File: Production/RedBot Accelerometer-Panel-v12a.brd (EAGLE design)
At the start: 129 x 137.2 mm, 915 parts, among them U1 MMA8452QMMA8452Q-1:1, U10 PCA9306, U100 PCA9306, U101 MMA8452QMMA8452Q-1:1, U102 MIC5205-3.3V, U103 PCA9306, U104 MMA8452QMMA8452Q-1:1, U105 MIC5205-3.3V, U106 PCA9306, U107 MMA8452QMMA8452Q-1:1, U108 MIC5205-3.3V, U109 PCA9306, U11 MMA8452QMMA8452Q-1:1, U110 MMA8452QMMA8452Q-1:1, U111 MIC5205-3.3V, U112 PCA9306, U113 MMA8452QMMA8452Q-1:1, U114 MIC5205-3.3V, U115 PCA9306, U116 MMA8452QMMA8452Q-1:1, U117 MIC5205-3.3V, U118 PCA9306, U119 MMA8452QMMA8452Q-1:1, U12 MIC5205-3.3V, U120 MIC5205-3.3V, U121 PCA9306, U122 MMA8452QMMA8452Q-1:1, U123 MIC5205-3.3V, U124 PCA9306, U125 MMA8452QMMA8452Q-1:1, U126 MIC5205-3.3V, U127 PCA9306, U128 MMA8452QMMA8452Q-1:1, U129 MIC5205-3.3V, U13 PCA9306, U130 PCA9306, U131 MMA8452QMMA8452Q-1:1, U132 MIC5205-3.3V, U133 PCA9306, U134 MMA8452QMMA8452Q-1:1, U135 MIC5205-3.3V, U136 PCA9306, U137 MMA8452QMMA8452Q-1:1, U138 MIC5205-3.3V, U139 PCA9306, U14 MMA8452QMMA8452Q-1:1, U140 MMA8452QMMA8452Q-1:1, U141 MIC5205-3.3V, U142 PCA9306, U143 MMA8452QMMA8452Q-1:1, U144 MIC5205-3.3V, U15 MIC5205-3.3V, U16 PCA9306, U17 MMA8452QMMA8452Q-1:1, U18 MIC5205-3.3V, U19 PCA9306, U2 MIC5205-3.3V, U20 MMA8452QMMA8452Q-1:1, U21 MIC5205-3.3V, U22 PCA9306, U23 MMA8452QMMA8452Q-1:1, U24 MIC5205-3.3V, U25 PCA9306, U26 MMA8452QMMA8452Q-1:1, U27 MIC5205-3.3V, U28 PCA9306, U29 MMA8452QMMA8452Q-1:1, U3 PCA9306, U30 MIC5205-3.3V, U31 PCA9306, U32 MMA8452QMMA8452Q-1:1, U33 MIC5205-3.3V, U34 PCA9306, U35 MMA8452QMMA8452Q-1:1, U36 MIC5205-3.3V, U37 PCA9306, U38 MMA8452QMMA8452Q-1:1, U39 MIC5205-3.3V, U4 PCA9306, U40 PCA9306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

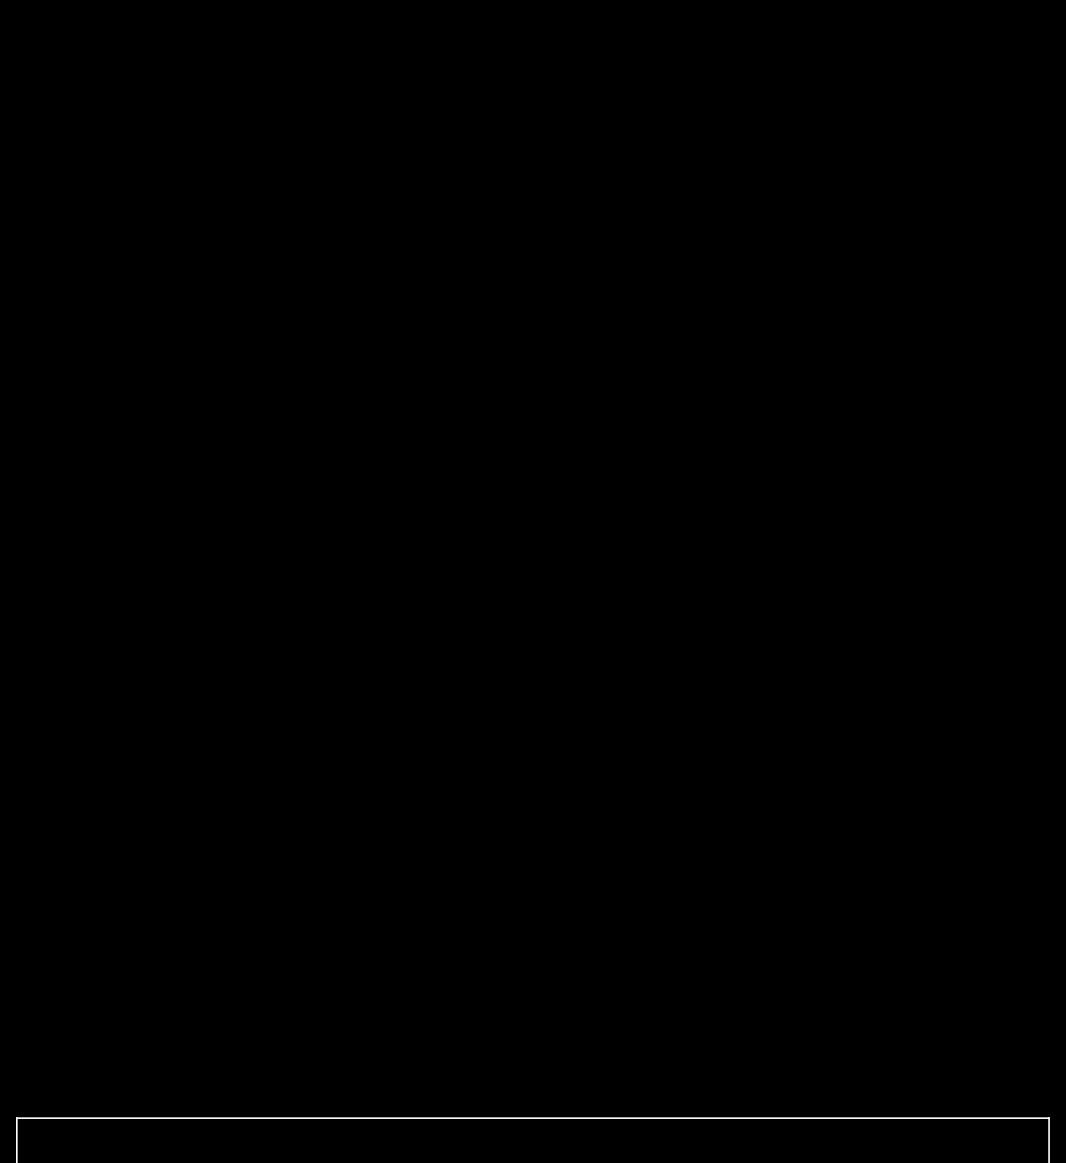
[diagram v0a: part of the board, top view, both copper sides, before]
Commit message: created large v12a panel
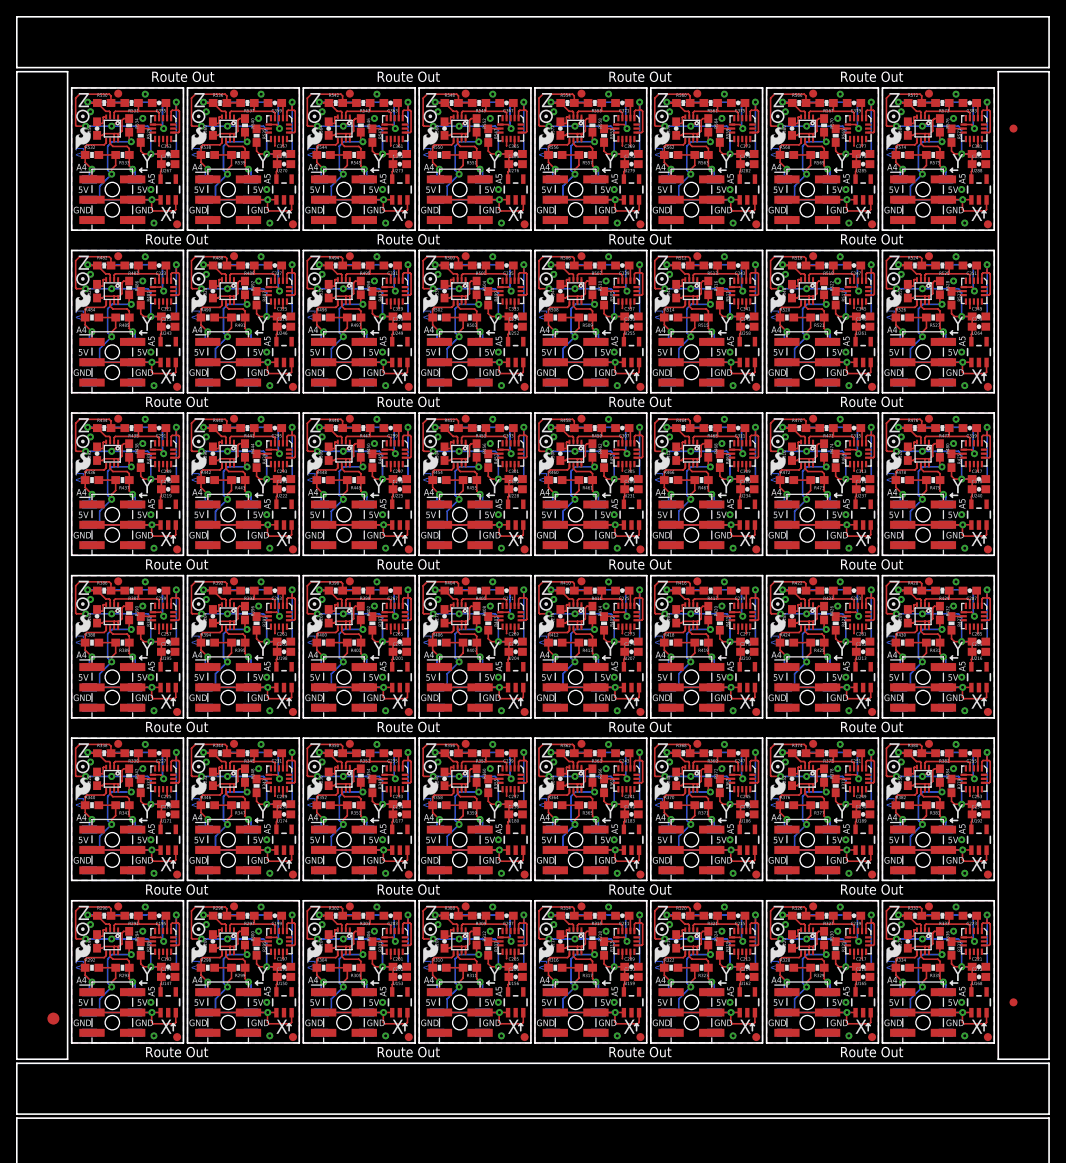
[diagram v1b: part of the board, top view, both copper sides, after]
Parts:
- added C193, C195, C196, C197, C199, C200, C201, C203, C204, C205, C207, C208, C209, C211, C212, C213, C215, C216, C217, C219, C220, C221, C223, C224, C225, C227, C228, C229, C231, C232, C233, C235, C236, C237, C239, C240, C241, C243, C244, C245, C247, C248, C249, C251, C252, C253, C255, C256, C257, C259, C260, C261, C263, C264, C265, C267, C268, C269, C271, C272, C273, C275, C276, C277, C279, C280, C281, C283, C284, C285, C287, C288, C289, C291, C292, C293, C295, C296, C297, C299, C300, C301, C303, C304, C305, C307, C308, C309, C311, C312, C313, C315, C316, C317, C319, C320, C321, C323, C324, C325, C327, C328, C329, C331, C332, C333, C335, C336, C337, C339, C340, C341, C343, C344, C345, C347, C348, C349, C351, C352, C353, C355, C356, C357, C359, C360, C361, C363, C364, C365, C367, C368, C369, C371, C372, C373, C375, C376, C377, C379, C380, C381, C383, C384: 0.1uF, SparkFun-Capacitors:0603-CAP
- added C194, C198, C202, C206, C210, C214, C218, C222, C226, C230, C234, C238, C242, C246, C250, C254, C258, C262, C266, C270, C274, C278, C282, C286, C290, C294, C298, C302, C306, C310, C314, C318, C322, C326, C330, C334, C338, C342, C346, C350, C354, C358, C362, C366, C370, C374, C378, C382: 4.7uF, SparkFun-Capacitors:0603-CAP
- added E$4, E$5: (no value), SparkFun-Aesthetics:FIDUCIAL-1X2
- added E$6: (no value), SparkFun-Retired:FIDUCIAL-1.5X3
- added FID100, FID101, FID102, FID103, FID104, FID105, FID106, FID107, FID108, FID109, FID110, FID111, FID112, FID113, FID114, FID115, FID116, FID117, FID118, FID119, FID120, FID121, FID122, FID123, FID124, FID125, FID126, FID127, FID128, FID129, FID130, FID131, FID132, FID133, FID134, FID135, FID136, FID137, FID138, FID139, FID140, FID141, FID142, FID143, FID144, FID145, FID146, FID147, FID148, FID149, FID150, FID151, FID152, FID153, FID154, FID155, FID156, FID157, FID158, FID159, FID160, FID161, FID162, FID163, FID164, FID165, FID166, FID167, FID168, FID169, FID170, FID171, FID172, FID173, FID174, FID175, FID176, FID177, FID178, FID179, FID180, FID181, FID182, FID183, FID184, FID185, FID186, FID187, FID188, FID189, FID190, FID191, FID192, FID97, FID98, FID99: FIDUCIAL1X2, SparkFun-Aesthetics:FIDUCIAL-1X2
- added JP100, JP102, JP104, JP106, JP108, JP110, JP112, JP114, JP116, JP118, JP120, JP122, JP124, JP126, JP128, JP130, JP132, JP134, JP136, JP138, JP140, JP142, JP144, JP146, JP148, JP150, JP152, JP154, JP156, JP158, JP160, JP162, JP164, JP166, JP168, JP170, JP172, JP174, JP176, JP178, JP180, JP182, JP184, JP186, JP188, JP190, JP192, JP98: (no value), SparkFun-Connectors:2X3_SMD
- added JP101, JP103, JP105, JP107, JP109, JP111, JP113, JP115, JP117, JP119, JP121, JP123, JP125, JP127, JP129, JP131, JP133, JP135, JP137, JP139, JP141, JP143, JP145, JP147, JP149, JP151, JP153, JP155, JP157, JP159, JP161, JP163, JP165, JP167, JP169, JP171, JP173, JP175, JP177, JP179, JP181, JP183, JP185, JP187, JP189, JP191, JP97, JP99: (no value), SparkFun-Connectors:2X3_SMT_POSTS
- added LOGO100, LOGO102, LOGO104, LOGO106, LOGO108, LOGO110, LOGO112, LOGO114, LOGO116, LOGO118, LOGO120, LOGO122, LOGO124, LOGO126, LOGO128, LOGO130, LOGO132, LOGO134, LOGO136, LOGO138, LOGO140, LOGO142, LOGO144, LOGO146, LOGO148, LOGO150, LOGO152, LOGO154, LOGO156, LOGO158, LOGO160, LOGO162, LOGO164, LOGO166, LOGO168, LOGO170, LOGO172, LOGO174, LOGO176, LOGO178, LOGO180, LOGO182, LOGO184, LOGO186, LOGO188, LOGO190, LOGO192, LOGO98: OSHW-LOGOS, SparkFun-Aesthetics:OSHW-LOGO-S
- added LOGO101, LOGO103, LOGO105, LOGO107, LOGO109, LOGO111, LOGO113, LOGO115, LOGO117, LOGO119, LOGO121, LOGO123, LOGO125, LOGO127, LOGO129, LOGO131, LOGO133, LOGO135, LOGO137, LOGO139, LOGO141, LOGO143, LOGO145, LOGO147, LOGO149, LOGO151, LOGO153, LOGO155, LOGO157, LOGO159, LOGO161, LOGO163, LOGO165, LOGO167, LOGO169, LOGO171, LOGO173, LOGO175, LOGO177, LOGO179, LOGO181, LOGO183, LOGO185, LOGO187, LOGO189, LOGO191, LOGO97, LOGO99: LOGO-SFESK, SparkFun-Aesthetics:SFE-LOGO-FLAME
- added R289, R295, R301, R307, R313, R319, R325, R331, R337, R343, R349, R355, R361, R367, R373, R379, R385, R391, R397, R403, R409, R415, R421, R427, R433, R439, R445, R451, R457, R463, R469, R475, R481, R487, R493, R499, R505, R511, R517, R523, R529, R535, R541, R547, R553, R559, R565, R571: 10k, SparkFun-Resistors:0603-RES
- added R290, R291, R292, R293, R296, R297, R298, R299, R302, R303, R304, R305, R308, R309, R310, R311, R314, R315, R316, R317, R320, R321, R322, R323, R326, R327, R328, R329, R332, R333, R334, R335, R338, R339, R340, R341, R344, R345, R346, R347, R350, R351, R352, R353, R356, R357, R358, R359, R362, R363, R364, R365, R368, R369, R370, R371, R374, R375, R376, R377, R380, R381, R382, R383, R386, R387, R388, R389, R392, R393, R394, R395, R398, R399, R400, R401, R404, R405, R406, R407, R410, R411, R412, R413, R416, R417, R418, R419, R422, R423, R424, R425, R428, R429, R430, R431, R434, R435, R436, R437, R440, R441, R442, R443, R446, R447, R448, R449, R452, R453, R454, R455, R458, R459, R460, R461, R464, R465, R466, R467, R470, R471, R472, R473, R476, R477, R478, R479, R482, R483, R484, R485, R488, R489, R490, R491, R494, R495, R496, R497, R500, R501, R502, R503, R506, R507, R508, R509, R512, R513, R514, R515, R518, R519, R520, R521, R524, R525, R526, R527, R530, R531, R532, R533, R536, R537, R538, R539, R542, R543, R544, R545, R548, R549, R550, R551, R554, R555, R556, R557, R560, R561, R562, R563, R566, R567, R568, R569, R572, R573, R574, R575: 1k, SparkFun-Resistors:0603-RES
- added R294, R300, R306, R312, R318, R324, R330, R336, R342, R348, R354, R360, R366, R372, R378, R384, R390, R396, R402, R408, R414, R420, R426, R432, R438, R444, R450, R456, R462, R468, R474, R480, R486, R492, R498, R504, R510, R516, R522, R528, R534, R540, R546, R552, R558, R564, R570, R576: 200k, SparkFun-Resistors:0603-RES
- added U145, U148, U151, U154, U157, U160, U163, U166, U169, U172, U175, U178, U181, U184, U187, U190, U193, U196, U199, U202, U205, U208, U211, U214, U217, U220, U223, U226, U229, U232, U235, U238, U241, U244, U247, U250, U253, U256, U259, U262, U265, U268, U271, U274, U277, U280, U283, U286: PCA9306, SparkFun-DigitalIC:PCA9306DC-1:1
- added U146, U149, U152, U155, U158, U161, U164, U167, U170, U173, U176, U179, U182, U185, U188, U191, U194, U197, U200, U203, U206, U209, U212, U215, U218, U221, U224, U227, U230, U233, U236, U239, U242, U245, U248, U251, U254, U257, U260, U263, U266, U269, U272, U275, U278, U281, U284, U287: MMA8452QMMA8452Q-1:1, SparkFun-Sensors:MMA8452Q-1:1
- added U147, U150, U153, U156, U159, U162, U165, U168, U171, U174, U177, U180, U183, U186, U189, U192, U195, U198, U201, U204, U207, U210, U213, U216, U219, U222, U225, U228, U231, U234, U237, U240, U243, U246, U249, U252, U255, U258, U261, U264, U267, U270, U273, U276, U279, U282, U285, U288: MIC5205-3.3V, SparkFun-PowerIC:SOT23-5
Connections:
- new net 3.3V48: C193.1, C194.1, R289.2, R290.2, R291.2, U145.1, U146.1, U146.14, U147.5
- new net 3.3V49: C197.1, C198.1, R295.2, R296.2, R297.2, U148.1, U149.1, U149.14, U150.5
- new net 3.3V50: C201.1, C202.1, R301.2, R302.2, R303.2, U151.1, U152.1, U152.14, U153.5
- new net 3.3V51: C205.1, C206.1, R307.2, R308.2, R309.2, U154.1, U155.1, U155.14, U156.5
- new net 3.3V52: C209.1, C210.1, R313.2, R314.2, R315.2, U157.1, U158.1, U158.14, U159.5
- new net 3.3V53: C213.1, C214.1, R319.2, R320.2, R321.2, U160.1, U161.1, U161.14, U162.5
- new net 3.3V54: C217.1, C218.1, R325.2, R326.2, R327.2, U163.1, U164.1, U164.14, U165.5
- new net 3.3V55: C221.1, C222.1, R331.2, R332.2, R333.2, U166.1, U167.1, U167.14, U168.5
- new net 3.3V56: C225.1, C226.1, R337.2, R338.2, R339.2, U169.1, U170.1, U170.14, U171.5
- new net 3.3V57: C229.1, C230.1, R343.2, R344.2, R345.2, U172.1, U173.1, U173.14, U174.5
- new net 3.3V58: C233.1, C234.1, R349.2, R350.2, R351.2, U175.1, U176.1, U176.14, U177.5
- new net 3.3V59: C237.1, C238.1, R355.2, R356.2, R357.2, U178.1, U179.1, U179.14, U180.5
- new net 3.3V60: C241.1, C242.1, R361.2, R362.2, R363.2, U181.1, U182.1, U182.14, U183.5
- new net 3.3V61: C245.1, C246.1, R367.2, R368.2, R369.2, U184.1, U185.1, U185.14, U186.5
- new net 3.3V62: C249.1, C250.1, R373.2, R374.2, R375.2, U187.1, U188.1, U188.14, U189.5
- new net 3.3V63: C253.1, C254.1, R379.2, R380.2, R381.2, U190.1, U191.1, U191.14, U192.5
- new net 3.3V64: C257.1, C258.1, R385.2, R386.2, R387.2, U193.1, U194.1, U194.14, U195.5
- new net 3.3V65: C261.1, C262.1, R391.2, R392.2, R393.2, U196.1, U197.1, U197.14, U198.5
- new net 3.3V66: C265.1, C266.1, R397.2, R398.2, R399.2, U199.1, U200.1, U200.14, U201.5
- new net 3.3V67: C269.1, C270.1, R403.2, R404.2, R405.2, U202.1, U203.1, U203.14, U204.5
- new net 3.3V68: C273.1, C274.1, R409.2, R410.2, R411.2, U205.1, U206.1, U206.14, U207.5
- new net 3.3V69: C277.1, C278.1, R415.2, R416.2, R417.2, U208.1, U209.1, U209.14, U210.5
- new net 3.3V70: C281.1, C282.1, R421.2, R422.2, R423.2, U211.1, U212.1, U212.14, U213.5
- new net 3.3V71: C285.1, C286.1, R427.2, R428.2, R429.2, U214.1, U215.1, U215.14, U216.5
- new net 3.3V72: C289.1, C290.1, R433.2, R434.2, R435.2, U217.1, U218.1, U218.14, U219.5
- new net 3.3V73: C293.1, C294.1, R439.2, R440.2, R441.2, U220.1, U221.1, U221.14, U222.5
- new net 3.3V74: C297.1, C298.1, R445.2, R446.2, R447.2, U223.1, U224.1, U224.14, U225.5
- new net 3.3V75: C301.1, C302.1, R451.2, R452.2, R453.2, U226.1, U227.1, U227.14, U228.5
- new net 3.3V76: C305.1, C306.1, R457.2, R458.2, R459.2, U229.1, U230.1, U230.14, U231.5
- new net 3.3V77: C309.1, C310.1, R463.2, R464.2, R465.2, U232.1, U233.1, U233.14, U234.5
- new net 3.3V78: C313.1, C314.1, R469.2, R470.2, R471.2, U235.1, U236.1, U236.14, U237.5
- new net 3.3V79: C317.1, C318.1, R475.2, R476.2, R477.2, U238.1, U239.1, U239.14, U240.5
- new net 3.3V80: C321.1, C322.1, R481.2, R482.2, R483.2, U241.1, U242.1, U242.14, U243.5
- new net 3.3V81: C325.1, C326.1, R487.2, R488.2, R489.2, U244.1, U245.1, U245.14, U246.5
- new net 3.3V82: C329.1, C330.1, R493.2, R494.2, R495.2, U247.1, U248.1, U248.14, U249.5
- new net 3.3V83: C333.1, C334.1, R499.2, R500.2, R501.2, U250.1, U251.1, U251.14, U252.5
- new net 3.3V84: C337.1, C338.1, R505.2, R506.2, R507.2, U253.1, U254.1, U254.14, U255.5
- new net 3.3V85: C341.1, C342.1, R511.2, R512.2, R513.2, U256.1, U257.1, U257.14, U258.5
- new net 3.3V86: C345.1, C346.1, R517.2, R518.2, R519.2, U259.1, U260.1, U260.14, U261.5
- new net 3.3V87: C349.1, C350.1, R523.2, R524.2, R525.2, U262.1, U263.1, U263.14, U264.5
- new net 3.3V88: C353.1, C354.1, R529.2, R530.2, R531.2, U265.1, U266.1, U266.14, U267.5
- new net 3.3V89: C357.1, C358.1, R535.2, R536.2, R537.2, U268.1, U269.1, U269.14, U270.5
- new net 3.3V90: C361.1, C362.1, R541.2, R542.2, R543.2, U271.1, U272.1, U272.14, U273.5
- new net 3.3V91: C365.1, C366.1, R547.2, R548.2, R549.2, U274.1, U275.1, U275.14, U276.5
- new net 3.3V92: C369.1, C370.1, R553.2, R554.2, R555.2, U277.1, U278.1, U278.14, U279.5
- new net 3.3V93: C373.1, C374.1, R559.2, R560.2, R561.2, U280.1, U281.1, U281.14, U282.5
- new net 3.3V94: C377.1, C378.1, R565.2, R566.2, R567.2, U283.1, U284.1, U284.14, U285.5
- new net 3.3V95: C381.1, C382.1, R571.2, R572.2, R573.2, U286.1, U287.1, U287.14, U288.5
- new net 5V48: JP97.3, JP97.4, JP98.3, JP98.4, R292.2, R293.2, R294.2, U147.1, U147.3
- new net 5V49: JP100.3, JP100.4, JP99.3, JP99.4, R298.2, R299.2, R300.2, U150.1, U150.3
- new net 5V50: JP101.3, JP101.4, JP102.3, JP102.4, R304.2, R305.2, R306.2, U153.1, U153.3
- new net 5V51: JP103.3, JP103.4, JP104.3, JP104.4, R310.2, R311.2, R312.2, U156.1, U156.3
- new net 5V52: JP105.3, JP105.4, JP106.3, JP106.4, R316.2, R317.2, R318.2, U159.1, U159.3
- new net 5V53: JP107.3, JP107.4, JP108.3, JP108.4, R322.2, R323.2, R324.2, U162.1, U162.3
- new net 5V54: JP109.3, JP109.4, JP110.3, JP110.4, R328.2, R329.2, R330.2, U165.1, U165.3
- new net 5V55: JP111.3, JP111.4, JP112.3, JP112.4, R334.2, R335.2, R336.2, U168.1, U168.3
- new net 5V56: JP113.3, JP113.4, JP114.3, JP114.4, R340.2, R341.2, R342.2, U171.1, U171.3
- new net 5V57: JP115.3, JP115.4, JP116.3, JP116.4, R346.2, R347.2, R348.2, U174.1, U174.3
- new net 5V58: JP117.3, JP117.4, JP118.3, JP118.4, R352.2, R353.2, R354.2, U177.1, U177.3
- new net 5V59: JP119.3, JP119.4, JP120.3, JP120.4, R358.2, R359.2, R360.2, U180.1, U180.3
- new net 5V60: JP121.3, JP121.4, JP122.3, JP122.4, R364.2, R365.2, R366.2, U183.1, U183.3
- new net 5V61: JP123.3, JP123.4, JP124.3, JP124.4, R370.2, R371.2, R372.2, U186.1, U186.3
- new net 5V62: JP125.3, JP125.4, JP126.3, JP126.4, R376.2, R377.2, R378.2, U189.1, U189.3
- new net 5V63: JP127.3, JP127.4, JP128.3, JP128.4, R382.2, R383.2, R384.2, U192.1, U192.3
- new net 5V64: JP129.3, JP129.4, JP130.3, JP130.4, R388.2, R389.2, R390.2, U195.1, U195.3
- new net 5V65: JP131.3, JP131.4, JP132.3, JP132.4, R394.2, R395.2, R396.2, U198.1, U198.3
- new net 5V66: JP133.3, JP133.4, JP134.3, JP134.4, R400.2, R401.2, R402.2, U201.1, U201.3
- new net 5V67: JP135.3, JP135.4, JP136.3, JP136.4, R406.2, R407.2, R408.2, U204.1, U204.3
- new net 5V68: JP137.3, JP137.4, JP138.3, JP138.4, R412.2, R413.2, R414.2, U207.1, U207.3
- new net 5V69: JP139.3, JP139.4, JP140.3, JP140.4, R418.2, R419.2, R420.2, U210.1, U210.3
- new net 5V70: JP141.3, JP141.4, JP142.3, JP142.4, R424.2, R425.2, R426.2, U213.1, U213.3
- new net 5V71: JP143.3, JP143.4, JP144.3, JP144.4, R430.2, R431.2, R432.2, U216.1, U216.3
- new net 5V72: JP145.3, JP145.4, JP146.3, JP146.4, R436.2, R437.2, R438.2, U219.1, U219.3
- new net 5V73: JP147.3, JP147.4, JP148.3, JP148.4, R442.2, R443.2, R444.2, U222.1, U222.3
- new net 5V74: JP149.3, JP149.4, JP150.3, JP150.4, R448.2, R449.2, R450.2, U225.1, U225.3
- new net 5V75: JP151.3, JP151.4, JP152.3, JP152.4, R454.2, R455.2, R456.2, U228.1, U228.3
- new net 5V76: JP153.3, JP153.4, JP154.3, JP154.4, R460.2, R461.2, R462.2, U231.1, U231.3
- new net 5V77: JP155.3, JP155.4, JP156.3, JP156.4, R466.2, R467.2, R468.2, U234.1, U234.3
- new net 5V78: JP157.3, JP157.4, JP158.3, JP158.4, R472.2, R473.2, R474.2, U237.1, U237.3
- new net 5V79: JP159.3, JP159.4, JP160.3, JP160.4, R478.2, R479.2, R480.2, U240.1, U240.3
- new net 5V80: JP161.3, JP161.4, JP162.3, JP162.4, R484.2, R485.2, R486.2, U243.1, U243.3
- new net 5V81: JP163.3, JP163.4, JP164.3, JP164.4, R490.2, R491.2, R492.2, U246.1, U246.3
- new net 5V82: JP165.3, JP165.4, JP166.3, JP166.4, R496.2, R497.2, R498.2, U249.1, U249.3
- new net 5V83: JP167.3, JP167.4, JP168.3, JP168.4, R502.2, R503.2, R504.2, U252.1, U252.3
- new net 5V84: JP169.3, JP169.4, JP170.3, JP170.4, R508.2, R509.2, R510.2, U255.1, U255.3
- new net 5V85: JP171.3, JP171.4, JP172.3, JP172.4, R514.2, R515.2, R516.2, U258.1, U258.3
- new net 5V86: JP173.3, JP173.4, JP174.3, JP174.4, R520.2, R521.2, R522.2, U261.1, U261.3
- new net 5V87: JP175.3, JP175.4, JP176.3, JP176.4, R526.2, R527.2, R528.2, U264.1, U264.3
- new net 5V88: JP177.3, JP177.4, JP178.3, JP178.4, R532.2, R533.2, R534.2, U267.1, U267.3
- new net 5V89: JP179.3, JP179.4, JP180.3, JP180.4, R538.2, R539.2, R540.2, U270.1, U270.3
- new net 5V90: JP181.3, JP181.4, JP182.3, JP182.4, R544.2, R545.2, R546.2, U273.1, U273.3
- new net 5V91: JP183.3, JP183.4, JP184.3, JP184.4, R550.2, R551.2, R552.2, U276.1, U276.3
- new net 5V92: JP185.3, JP185.4, JP186.3, JP186.4, R556.2, R557.2, R558.2, U279.1, U279.3
- new net 5V93: JP187.3, JP187.4, JP188.3, JP188.4, R562.2, R563.2, R564.2, U282.1, U282.3
- new net 5V94: JP189.3, JP189.4, JP190.3, JP190.4, R568.2, R569.2, R570.2, U285.1, U285.3
- new net 5V95: JP191.3, JP191.4, JP192.3, JP192.4, R574.2, R575.2, R576.2, U288.1, U288.3
- new net ADDR48: R289.1, U146.7
- new net ADDR49: R295.1, U149.7
- new net ADDR50: R301.1, U152.7
- new net ADDR51: R307.1, U155.7
- new net ADDR52: R313.1, U158.7
- new net ADDR53: R319.1, U161.7
- new net ADDR54: R325.1, U164.7
- new net ADDR55: R331.1, U167.7
- new net ADDR56: R337.1, U170.7
- new net ADDR57: R343.1, U173.7
- new net ADDR58: R349.1, U176.7
- new net ADDR59: R355.1, U179.7
- new net ADDR60: R361.1, U182.7
- new net ADDR61: R367.1, U185.7
- new net ADDR62: R373.1, U188.7
- new net ADDR63: R379.1, U191.7
- new net ADDR64: R385.1, U194.7
- new net ADDR65: R391.1, U197.7
- new net ADDR66: R397.1, U200.7
- new net ADDR67: R403.1, U203.7
- new net ADDR68: R409.1, U206.7
- new net ADDR69: R415.1, U209.7
- new net ADDR70: R421.1, U212.7
- new net ADDR71: R427.1, U215.7
- new net ADDR72: R433.1, U218.7
- new net ADDR73: R439.1, U221.7
- new net ADDR74: R445.1, U224.7
- new net ADDR75: R451.1, U227.7
- new net ADDR76: R457.1, U230.7
- new net ADDR77: R463.1, U233.7
- new net ADDR78: R469.1, U236.7
- new net ADDR79: R475.1, U239.7
- new net ADDR80: R481.1, U242.7
- new net ADDR81: R487.1, U245.7
- new net ADDR82: R493.1, U248.7
- new net ADDR83: R499.1, U251.7
- new net ADDR84: R505.1, U254.7
- new net ADDR85: R511.1, U257.7
- new net ADDR86: R517.1, U260.7
- new net ADDR87: R523.1, U263.7
- new net ADDR88: R529.1, U266.7
- new net ADDR89: R535.1, U269.7
- new net ADDR90: R541.1, U272.7
- new net ADDR91: R547.1, U275.7
- new net ADDR92: R553.1, U278.7
- new net ADDR93: R559.1, U281.7
- new net ADDR94: R565.1, U284.7
- new net ADDR95: R571.1, U287.7
- new net GND48: C193.2, C194.2, C195.2, C196.2, JP97.5, JP97.6, JP98.5, JP98.6, U145.4, U146.10, U146.12, U146.5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
- new net GND49: C197.2, C198.2, C199.2, C200.2, JP100.5, JP100.6, JP99.5, JP99.6, U148.4, U149.10, U149.12, U149.5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
- new net GND50: C201.2, C202.2, C203.2, C204.2, JP101.5, JP101.6, JP102.5, JP102.6, U151.4, U152.10, U152.12, U152.5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
- new net GND51: C205.2, C206.2, C207.2, C208.2, JP103.5, JP103.6, JP104.5, JP104.6, U154.4, U155.10, U155.12, U155.5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
- new net GND52: C209.2, C210.2, C211.2, C212.2, JP105.5, JP105.6, JP106.5, JP106.6, U157.4, U158.10, U158.12, U158.5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
- new net GND53: C213.2, C214.2, C215.2, C216.2, JP107.5, JP107.6, JP108.5, JP108.6, U160.4, U161.10, U161.12, U161.5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
- new net GND54: C217.2, C218.2, C219.2, C220.2, JP109.5, JP109.6, JP110.5, JP110.6, U163.4, U164.10, U164.12, U164.5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
- new net GND55: C221.2, C222.2, C223.2, C224.2, JP111.5, JP111.6, JP112.5, JP112.6, U166.4, U167.10, U167.12, U167.5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
- new net GND56: C225.2, C226.2, C227.2, C228.2, JP113.5, JP113.6, JP114.5, JP114.6, U169.4, U170.10, U170.12, U170.5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
- new net GND57: C229.2, C230.2, C231.2, C232.2, JP115.5, JP115.6, JP116.5, JP116.6, U172.4, U173.10, U173.12, U173.5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
- new net GND58: C233.2, C234.2, C235.2, C236.2, JP117.5, JP117.6, JP118.5, JP118.6, U175.4, U176.10, U176.12, U176.5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
- new net GND59: C237.2, C238.2, C239.2, C240.2, JP119.5, JP119.6, JP120.5, JP120.6, U178.4, U179.10, U179.12, U179.5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
- new net GND60: C241.2, C242.2, C243.2, C244.2, JP121.5, JP121.6, JP122.5, JP122.6, U181.4, U182.10, U182.12, U182.5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
- new net GND61: C245.2, C246.2, C247.2, C248.2, JP123.5, JP123.6, JP124.5, JP124.6, U184.4, U185.10, U185.12, U185.5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
- new net GND62: C249.2, C250.2, C251.2, C252.2, JP125.5, JP125.6, JP126.5, JP126.6, U187.4, U188.10, U188.12, U188.5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
- new net GND63: C253.2, C254.2, C255.2, C256.2, JP127.5, JP127.6, JP128.5, JP128.6, U190.4, U191.10, U191.12, U191.5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
- new net GND64: C257.2, C258.2, C259.2, C260.2, JP129.5, JP129.6, JP130.5, JP130.6, U193.4, U194.10, U194.12, U194.5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
- new net GND65: C261.2, C262.2, C263.2, C264.2, JP131.5, JP131.6, JP132.5, JP132.6, U196.4, U197.10, U197.12, U197.5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
- new net GND66: C265.2, C266.2, C267.2, C268.2, JP133.5, JP133.6, JP134.5, JP134.6, U199.4, U200.10, U200.12, U200.5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
- new net GND67: C269.2, C270.2, C271.2, C272.2, JP135.5, JP135.6, JP136.5, JP136.6, U202.4, U203.10, U203.12, U203.5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
- new net GND68: C273.2, C274.2, C275.2, C276.2, JP137.5, JP137.6, JP138.5, JP138.6, U205.4, U206.10, U206.12, U206.5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
- new net GND69: C277.2, C278.2, C279.2, C280.2, JP139.5, JP139.6, JP140.5, JP140.6, U208.4, U209.10, U209.12, U209.5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
- new net GND70: C281.2, C282.2, C283.2, C284.2, JP141.5, JP141.6, JP142.5, JP142.6, U211.4, U212.10, U212.12, U212.5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
- new net GND71: C285.2, C286.2, C287.2, C288.2, JP143.5, JP143.6, JP144.5, JP144.6, U214.4, U215.10, U215.12, U215.5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
- new net GND72: C289.2, C290.2, C291.2, C292.2, JP145.5, JP145.6, JP146.5, JP146.6, U217.4, U218.10, U218.12, U218.5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
- new net GND73: C293.2, C294.2, C295.2, C296.2, JP147.5, JP147.6, JP148.5, JP148.6, U220.4, U221.10, U221.12, U221.5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
- new net GND74: C297.2, C298.2, C299.2, C300.2, JP149.5, JP149.6, JP150.5, JP150.6, U223.4, U224.10, U224.12, U224.5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
- new net GND75: C301.2, C302.2, C303.2, C304.2, JP151.5, JP151.6, JP152.5, JP152.6, U226.4, U227.10, U227.12, U227.5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
- new net GND76: C305.2, C306.2, C307.2, C308.2, JP153.5, JP153.6, JP154.5, JP154.6, U229.4, U230.10, U230.12, U230.5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
- new net GND77: C309.2, C310.2, C311.2, C312.2, JP155.5, JP155.6, JP156.5, JP156.6, U232.4, U233.10, U233.12, U233.5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
- new net GND78: C313.2, C314.2, C315.2, C316.2, JP157.5, JP157.6, JP158.5, JP158.6, U235.4, U236.10, U236.12, U236.5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
- new net GND79: C317.2, C318.2, C319.2, C320.2, JP159.5, JP159.6, JP160.5, JP160.6, U238.4, U239.10, U239.12, U239.5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
- new net GND80: C321.2, C322.2, C323.2, C324.2, JP161.5, JP161.6, JP162.5, JP162.6, U241.4, U242.10, U242.12, U242.5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
- new net GND81: C325.2, C326.2, C327.2, C328.2, JP163.5, JP163.6, JP164.5, JP164.6, U244.4, U245.10, U245.12, U245.5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
- new net GND82: C329.2, C330.2, C331.2, C332.2, JP165.5, JP165.6, JP166.5, JP166.6, U247.4, U248.10, U248.12, U248.5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
- new net GND83: C333.2, C334.2, C335.2, C336.2, JP167.5, JP167.6, JP168.5, JP168.6, U250.4, U251.10, U251.12, U251.5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
- new net GND84: C337.2, C338.2, C339.2, C340.2, JP169.5, JP169.6, JP170.5, JP170.6, U253.4, U254.10, U254.12, U254.5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
- new net GND85: C341.2, C342.2, C343.2, C344.2, JP171.5, JP171.6, JP172.5, JP172.6, U256.4, U257.10, U257.12, U257.5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
- new net GND86: C345.2, C346.2, C347.2, C348.2, JP173.5, JP173.6, JP174.5, JP174.6, U259.4, U260.10, U260.12, U260.5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
- new net GND87: C349.2, C350.2, C351.2, C352.2, JP175.5, JP175.6, JP176.5, JP176.6, U262.4, U263.10, U263.12, U263.5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
- new net GND88: C353.2, C354.2, C355.2, C356.2, JP177.5, JP177.6, JP178.5, JP178.6, U265.4, U266.10, U266.12, U266.5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
- new net GND89: C357.2, C358.2, C359.2, C360.2, JP179.5, JP179.6, JP180.5, JP180.6, U268.4, U269.10, U269.12, U269.5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
- new net GND90: C361.2, C362.2, C363.2, C364.2, JP181.5, JP181.6, JP182.5, JP182.6, U271.4, U272.10, U272.12, U272.5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
- new net GND91: C365.2, C366.2, C367.2, C368.2, JP183.5, JP183.6, JP184.5, JP184.6, U274.4, U275.10, U275.12, U275.5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
- new net GND92: C369.2, C370.2, C371.2, C372.2, JP185.5, JP185.6, JP186.5, JP186.6, U277.4, U278.10, U278.12, U278.5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
- new net GND93: C373.2, C374.2, C375.2, C376.2, JP187.5, JP187.6, JP188.5, JP188.6, U280.4, U281.10, U281.12, U281.5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
- new net GND94: C377.2, C378.2, C379.2, C380.2, JP189.5, JP189.6, JP190.5, JP190.6, U283.4, U284.10, U284.12, U284.5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
- new net GND95: C381.2, C382.2, C383.2, C384.2, JP191.5, JP191.6, JP192.5, JP192.6, U286.4, U287.10, U287.12, U287.5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
- new net N$100: C199.1, U149.2
- new net N$101: C204.1, R306.1, U151.7, U151.8
- new net N$102: C203.1, U152.2
- new net N$103: C208.1, R312.1, U154.7, U154.8
- new net N$104: C207.1, U155.2
- new net N$105: C212.1, R318.1, U157.7, U157.8
- new net N$106: C211.1, U158.2
- new net N$107: C216.1, R324.1, U160.7, U160.8
- new net N$108: C215.1, U161.2
- new net N$109: C220.1, R330.1, U163.7, U163.8
- new net N$110: C219.1, U164.2
- new net N$111: C224.1, R336.1, U166.7, U166.8
- new net N$112: C223.1, U167.2
- new net N$113: C228.1, R342.1, U169.7, U169.8
- new net N$114: C227.1, U170.2
- new net N$115: C232.1, R348.1, U172.7, U172.8
- new net N$116: C231.1, U173.2
- new net N$117: C236.1, R354.1, U175.7, U175.8
- new net N$118: C235.1, U176.2
- new net N$119: C240.1, R360.1, U178.7, U178.8
- new net N$120: C239.1, U179.2
- new net N$121: C244.1, R366.1, U181.7, U181.8
- new net N$122: C243.1, U182.2
- new net N$123: C248.1, R372.1, U184.7, U184.8
- new net N$124: C247.1, U185.2
- new net N$125: C252.1, R378.1, U187.7, U187.8
- new net N$126: C251.1, U188.2
- new net N$127: C256.1, R384.1, U190.7, U190.8
- new net N$128: C255.1, U191.2
- new net N$129: C260.1, R390.1, U193.7, U193.8
- new net N$130: C259.1, U194.2
- new net N$131: C264.1, R396.1, U196.7, U196.8
- new net N$132: C263.1, U197.2
- new net N$133: C268.1, R402.1, U199.7, U199.8
- new net N$134: C267.1, U200.2
- new net N$135: C272.1, R408.1, U202.7, U202.8
- new net N$136: C271.1, U203.2
- new net N$137: C276.1, R414.1, U205.7, U205.8
- new net N$138: C275.1, U206.2
- new net N$139: C280.1, R420.1, U208.7, U208.8
- new net N$140: C279.1, U209.2
- new net N$141: C284.1, R426.1, U211.7, U211.8
- new net N$142: C283.1, U212.2
- new net N$143: C288.1, R432.1, U214.7, U214.8
- new net N$144: C287.1, U215.2
- new net N$145: C292.1, R438.1, U217.7, U217.8
- new net N$146: C291.1, U218.2
- new net N$147: C296.1, R444.1, U220.7, U220.8
- new net N$148: C295.1, U221.2
- new net N$149: C300.1, R450.1, U223.7, U223.8
- new net N$150: C299.1, U224.2
- new net N$151: C304.1, R456.1, U226.7, U226.8
- new net N$152: C303.1, U227.2
- new net N$153: C308.1, R462.1, U229.7, U229.8
- new net N$154: C307.1, U230.2
- new net N$155: C312.1, R468.1, U232.7, U232.8
- new net N$156: C311.1, U233.2
- new net N$157: C316.1, R474.1, U235.7, U235.8
- new net N$158: C315.1, U236.2
- new net N$159: C320.1, R480.1, U238.7, U238.8
- new net N$160: C319.1, U239.2
- new net N$161: C324.1, R486.1, U241.7, U241.8
- new net N$162: C323.1, U242.2
- new net N$163: C328.1, R492.1, U244.7, U244.8
- new net N$164: C327.1, U245.2
- new net N$165: C332.1, R498.1, U247.7, U247.8
- new net N$166: C331.1, U248.2
- new net N$167: C336.1, R504.1, U250.7, U250.8
- new net N$168: C335.1, U251.2
- new net N$169: C340.1, R510.1, U253.7, U253.8
- new net N$170: C339.1, U254.2
- new net N$171: C344.1, R516.1, U256.7, U256.8
- new net N$172: C343.1, U257.2
- new net N$173: C348.1, R522.1, U259.7, U259.8
- new net N$174: C347.1, U260.2
- new net N$175: C352.1, R528.1, U262.7, U262.8
- new net N$176: C351.1, U263.2
- new net N$177: C356.1, R534.1, U265.7, U265.8
- new net N$178: C355.1, U266.2
- new net N$179: C360.1, R540.1, U268.7, U268.8
- new net N$180: C359.1, U269.2
- new net N$181: C364.1, R546.1, U271.7, U271.8
- new net N$182: C363.1, U272.2
- new net N$183: C368.1, R552.1, U274.7, U274.8
- new net N$184: C367.1, U275.2
- new net N$185: C372.1, R558.1, U277.7, U277.8
- new net N$186: C371.1, U278.2
- new net N$187: C376.1, R564.1, U280.7, U280.8
- new net N$188: C375.1, U281.2
- new net N$189: C380.1, R570.1, U283.7, U283.8
- new net N$190: C379.1, U284.2
- new net N$191: C384.1, R576.1, U286.7, U286.8
- new net N$192: C383.1, U287.2
- new net N$97: C196.1, R294.1, U145.7, U145.8
- new net N$98: C195.1, U146.2
- new net N$99: C200.1, R300.1, U148.7, U148.8
- new net SCL100: JP101.2, JP102.1, R305.1, U151.6
- new net SCL101: R303.1, U151.2, U152.4
- new net SCL102: JP103.2, JP104.1, R311.1, U154.6
- new net SCL103: R309.1, U154.2, U155.4
- new net SCL104: JP105.2, JP106.1, R317.1, U157.6
- new net SCL105: R315.1, U157.2, U158.4
- new net SCL106: JP107.2, JP108.1, R323.1, U160.6
- new net SCL107: R321.1, U160.2, U161.4
- new net SCL108: JP109.2, JP110.1, R329.1, U163.6
- new net SCL109: R327.1, U163.2, U164.4
- new net SCL110: JP111.2, JP112.1, R335.1, U166.6
- new net SCL111: R333.1, U166.2, U167.4
- new net SCL112: JP113.2, JP114.1, R341.1, U169.6
- new net SCL113: R339.1, U169.2, U170.4
- new net SCL114: JP115.2, JP116.1, R347.1, U172.6
- new net SCL115: R345.1, U172.2, U173.4
- new net SCL116: JP117.2, JP118.1, R353.1, U175.6
- new net SCL117: R351.1, U175.2, U176.4
- new net SCL118: JP119.2, JP120.1, R359.1, U178.6
- new net SCL119: R357.1, U178.2, U179.4
- new net SCL120: JP121.2, JP122.1, R365.1, U181.6
- new net SCL121: R363.1, U181.2, U182.4
- new net SCL122: JP123.2, JP124.1, R371.1, U184.6
- new net SCL123: R369.1, U184.2, U185.4
- new net SCL124: JP125.2, JP126.1, R377.1, U187.6
- new net SCL125: R375.1, U187.2, U188.4
- new net SCL126: JP127.2, JP128.1, R383.1, U190.6
- new net SCL127: R381.1, U190.2, U191.4
- new net SCL128: JP129.2, JP130.1, R389.1, U193.6
- new net SCL129: R387.1, U193.2, U194.4
- new net SCL130: JP131.2, JP132.1, R395.1, U196.6
- new net SCL131: R393.1, U196.2, U197.4
- new net SCL132: JP133.2, JP134.1, R401.1, U199.6
- new net SCL133: R399.1, U199.2, U200.4
- new net SCL134: JP135.2, JP136.1, R407.1, U202.6
- new net SCL135: R405.1, U202.2, U203.4
- new net SCL136: JP137.2, JP138.1, R413.1, U205.6
- new net SCL137: R411.1, U205.2, U206.4
- new net SCL138: JP139.2, JP140.1, R419.1, U208.6
- new net SCL139: R417.1, U208.2, U209.4
- new net SCL140: JP141.2, JP142.1, R425.1, U211.6
- new net SCL141: R423.1, U211.2, U212.4
- new net SCL142: JP143.2, JP144.1, R431.1, U214.6
- new net SCL143: R429.1, U214.2, U215.4
- new net SCL144: JP145.2, JP146.1, R437.1, U217.6
- new net SCL145: R435.1, U217.2, U218.4
- new net SCL146: JP147.2, JP148.1, R443.1, U220.6
- new net SCL147: R441.1, U220.2, U221.4
- new net SCL148: JP149.2, JP150.1, R449.1, U223.6
- new net SCL149: R447.1, U223.2, U224.4
- new net SCL150: JP151.2, JP152.1, R455.1, U226.6
- new net SCL151: R453.1, U226.2, U227.4
- new net SCL152: JP153.2, JP154.1, R461.1, U229.6
- new net SCL153: R459.1, U229.2, U230.4
- new net SCL154: JP155.2, JP156.1, R467.1, U232.6
- new net SCL155: R465.1, U232.2, U233.4
- new net SCL156: JP157.2, JP158.1, R473.1, U235.6
- new net SCL157: R471.1, U235.2, U236.4
- new net SCL158: JP159.2, JP160.1, R479.1, U238.6
- new net SCL159: R477.1, U238.2, U239.4
- new net SCL160: JP161.2, JP162.1, R485.1, U241.6
- new net SCL161: R483.1, U241.2, U242.4
- new net SCL162: JP163.2, JP164.1, R491.1, U244.6
- new net SCL163: R489.1, U244.2, U245.4
- new net SCL164: JP165.2, JP166.1, R497.1, U247.6
- new net SCL165: R495.1, U247.2, U248.4
- new net SCL166: JP167.2, JP168.1, R503.1, U250.6
- new net SCL167: R501.1, U250.2, U251.4
- new net SCL168: JP169.2, JP170.1, R509.1, U253.6
- new net SCL169: R507.1, U253.2, U254.4
- new net SCL170: JP171.2, JP172.1, R515.1, U256.6
- new net SCL171: R513.1, U256.2, U257.4
- new net SCL172: JP173.2, JP174.1, R521.1, U259.6
- new net SCL173: R519.1, U259.2, U260.4
- new net SCL174: JP175.2, JP176.1, R527.1, U262.6
- new net SCL175: R525.1, U262.2, U263.4
- new net SCL176: JP177.2, JP178.1, R533.1, U265.6
- new net SCL177: R531.1, U265.2, U266.4
- new net SCL178: JP179.2, JP180.1, R539.1, U268.6
- new net SCL179: R537.1, U268.2, U269.4
- new net SCL180: JP181.2, JP182.1, R545.1, U271.6
- new net SCL181: R543.1, U271.2, U272.4
- new net SCL182: JP183.2, JP184.1, R551.1, U274.6
- new net SCL183: R549.1, U274.2, U275.4
- new net SCL184: JP185.2, JP186.1, R557.1, U277.6
- new net SCL185: R555.1, U277.2, U278.4
- new net SCL186: JP187.2, JP188.1, R563.1, U280.6
- new net SCL187: R561.1, U280.2, U281.4
- new net SCL188: JP189.2, JP190.1, R569.1, U283.6
- new net SCL189: R567.1, U283.2, U284.4
- new net SCL190: JP191.2, JP192.1, R575.1, U286.6
- new net SCL191: R573.1, U286.2, U287.4
- new net SCL96: JP97.2, JP98.1, R293.1, U145.6
- new net SCL97: R291.1, U145.2, U146.4
- new net SCL98: JP100.1, JP99.2, R299.1, U148.6
- new net SCL99: R297.1, U148.2, U149.4
- new net SDA100: JP101.1, JP102.2, R304.1, U151.5
- new net SDA101: R302.1, U151.3, U152.6
- new net SDA102: JP103.1, JP104.2, R310.1, U154.5
- new net SDA103: R308.1, U154.3, U155.6
- new net SDA104: JP105.1, JP106.2, R316.1, U157.5
- new net SDA105: R314.1, U157.3, U158.6
- new net SDA106: JP107.1, JP108.2, R322.1, U160.5
- new net SDA107: R320.1, U160.3, U161.6
- new net SDA108: JP109.1, JP110.2, R328.1, U163.5
- new net SDA109: R326.1, U163.3, U164.6
- new net SDA110: JP111.1, JP112.2, R334.1, U166.5
- new net SDA111: R332.1, U166.3, U167.6
- new net SDA112: JP113.1, JP114.2, R340.1, U169.5
- new net SDA113: R338.1, U169.3, U170.6
- new net SDA114: JP115.1, JP116.2, R346.1, U172.5
- new net SDA115: R344.1, U172.3, U173.6
- new net SDA116: JP117.1, JP118.2, R352.1, U175.5
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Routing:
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- added copper zone on layer 1, net GND48
- added copper zone on layer 16, net GND48
- added copper zone on layer 1, net GND49
- added copper zone on layer 16, net GND49
- added copper zone on layer 1, net GND50
- added copper zone on layer 16, net GND50
- added copper zone on layer 1, net GND51
- added copper zone on layer 16, net GND51
- added copper zone on layer 1, net GND52
- added copper zone on layer 16, net GND52
- added copper zone on layer 1, net GND53
- added copper zone on layer 16, net GND53
- added copper zone on layer 1, net GND54
- added copper zone on layer 16, net GND54
- added copper zone on layer 1, net GND55
- added copper zone on layer 16, net GND55
- added copper zone on layer 1, net GND56
- added copper zone on layer 16, net GND56
- added copper zone on layer 1, net GND57
- added copper zone on layer 16, net GND57
- added copper zone on layer 1, net GND58
- added copper zone on layer 16, net GND58
- added copper zone on layer 1, net GND59
- added copper zone on layer 16, net GND59
- added copper zone on layer 1, net GND60
- added copper zone on layer 16, net GND60
- added copper zone on layer 1, net GND61
- added copper zone on layer 16, net GND61
- added copper zone on layer 1, net GND62
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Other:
- board size 129 x 137.2 mm -> 129 x 274.8 mm

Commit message: added bottom side panel fiducials
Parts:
- added E$10, E$12, E$8, E$9: (no value), SparkFun-Aesthetics:FIDUCIAL-1X2
- added E$11, E$7: (no value), SparkFun-Retired:FIDUCIAL-1.5X3
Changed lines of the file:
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@@
 <element name="E$5" library="SparkFun-Aesthetics" package="FIDUCIAL-1X2" value="" x="124.587" y="260.858" rot="R180"/>
 <element name="E$6" library="SparkFun-Retired" package="FIDUCIAL-1.5X3" value="" x="4.572" y="149.606"/>
+<element name="E$7" library="SparkFun-Retired" package="FIDUCIAL-1.5X3" value="" x="4.572" y="11.938" rot="MR0"/>
+<element name="E$8" library="SparkFun-Aesthetics" package="FIDUCIAL-1X2" value="" x="124.587" y="13.97" rot="MR0"/>
+<element name="E$9" library="SparkFun-Aesthetics" package="FIDUCIAL-1X2" value="" x="124.587" y="123.19" rot="MR180"/>
+<element name="E$10" library="SparkFun-Aesthetics" package="FIDUCIAL-1X2" value="" x="124.587" y="151.638" rot="MR0"/>
+<element name="E$11" library="SparkFun-Retired" package="FIDUCIAL-1.5X3" value="" x="4.572" y="149.606" rot="MR0"/>
+<element name="E$12" library="SparkFun-Aesthetics" package="FIDUCIAL-1X2" value="" x="124.587" y="260.858" rot="MR180"/>
 </elements>
 <signals>
